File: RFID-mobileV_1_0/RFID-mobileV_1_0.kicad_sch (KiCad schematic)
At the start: 5 parts

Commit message: 增加電池管理IC
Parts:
- removed F?: Fuse, Fuse:Fuse_0805_2012Metric, symbol Device:Fuse
- added U?: (no value), Package_TO_SOT_SMD:TSOT-23-5, symbol Battery_Management:TP4054
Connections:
- net +5V: now also J?.A4 (VBUS), J?.A9 (VBUS), J?.B4 (VBUS), J?.B9 (VBUS)
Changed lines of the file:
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@@
     (stroke (width 0) (type solid) (color 0 0 0 0))
   )
-  (wire (pts (xy 39.37 20.32) (xy 42.291 20.32))
-    (stroke (width 0) (type solid) (color 0 0 0 0))
-  )
-  (wire (pts (xy 49.911 20.32) (xy 52.07 20.32))
+  (wire (pts (xy 39.37 20.32) (xy 52.07 20.32))
     (stroke (width 0) (type solid) (color 0 0 0 0))
   )
@@
     (pin "S1")
   )
-  (symbol (lib_id "Device:Fuse") (at 46.101 20.32 90) (unit 1)
-    (in_bom yes) (on_board yes)
-    (property "Reference" "F?" (id 0) (at 46.101 15.3478 90))
-    (property "Value" "Fuse" (id 1) (at 46.101 17.6465 90))
-    (property "Footprint" "Fuse:Fuse_0805_2012Metric" (id 2) (at 46.101 22.098 90)
-      (effects (font (size 1.27 1.27)) hide)
-    )
-    (property "Datasheet" "~" (id 3) (at 46.101 20.32 0)
-      (effects (font (size 1.27 1.27)) hide)
-    )
-    (property "LCSC" "C135327" (id 4) (at 46.355 22.225 90))
-    (pin "1")
-    (pin "2")
-  )
   (symbol (lib_id "power:PWR_FLAG") (at 59.69 20.32 0) (unit 1)
     (in_bom yes) (on_board yes)
@@
     )
     (pin "1")
+  )
+  (symbol (lib_id "Battery_Management:TP4054") (at 76.2 135.255 0) (unit 1)
+    (in_bom yes) (on_board yes) (fields_autoplaced)
+    (property "Reference" "U?" (id 0) (at 85.725 127 0))
+    (property "Value" "" (id 1) (at 85.725 129.54 0))
+    (property "Footprint" "Package_TO_SOT_SMD:TSOT-23-5" (id 2) (at 87.63 144.145 0)
+      (effects (font (size 1.27 1.27)) hide)
+    )
+    (property "Datasheet" "" (id 3) (at 99.06 149.225 0)
+      (effects (font (size 1.27 1.27)) hide)
+    )
+    (property "LCSC" "C32574" (id 4) (at 96.52 131.445 0)
+      (effects (font (size 1.27 1.27)) (justify right) hide)
+    )
+    (pin "1")
+    (pin "2")
+    (pin "3")
+    (pin "4")
+    (pin "5")
   )
   (sheet_instances
@@
       (reference "BT?") (unit 1) (value "Battery") (footprint "")
     )
-    (path "/a647641f-bf16-4177-91ee-b01f347ff91c"
-      (reference "F?") (unit 1) (value "Fuse") (footprint "Fuse:Fuse_0805_2012Metric")
-    )
     (path "/a49e8613-3cd2-48ed-8977-6bb5023f7722"
       (reference "J?") (unit 1) (value "USB_C_Receptacle_USB2.0") (footprint "Connector_USB:USB_C_Receptacle_HRO_TYPE-C-31-M-12")
@@
       (reference "R?") (unit 1) (value "5K1") (footprint "Resistor_SMD:R_0805_2012Metric")
     )
-  )
+    (path "/cdc7c457-e16e-4018-ab8d-ab6698e85393"
+      (reference "U?") (unit 1) (value "TP4054") (footprint "Package_TO_SOT_SMD:TSOT-23-5")
+    )
+  )

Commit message: update sch
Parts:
- added BZ?: Buzzer, Buzzer_Beeper:Buzzer_Murata_PKLCS1212E, symbol Device:Buzzer
- added Q?: MMBT3904, Package_TO_SOT_SMD:SOT-23, symbol Transistor_BJT:MMBT3904
- added R?: 1k, Resistor_SMD:R_0805_2012Metric, symbol Device:R
- added R?: 22k, Resistor_SMD:R_0805_2012Metric, symbol Device:R
- added U?: (no value), symbol MCU_ST_STM32G0:STM32G030FxP
- added U?: (no value), symbol RF_Module:E220-400TxxS
- added U?: (no value), Package_TO_SOT_SMD:SOT-23-5, symbol Battery_Management:DW02
- BT?: value (none) -> Battery
- U?: value (none) -> TP4054
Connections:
- net +5V: now also BZ?.1 (-), R?.2
- net GND: now also Q?.2 (E)
- new net: BZ?.2 (+), Q?.3 (C), R?.1
- new net: Q?.1 (B), R?.1
- new net buz: R?.2

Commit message: Update RFID-mobileV_1_0.kicad_sch
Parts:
- U?: footprint (none) -> Package_SO:TSSOP-20_4.4x6.5mm_P0.65mm
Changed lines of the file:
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@@
     (property "Reference" "U?" (id 0) (at 142.875 30.48 0))
     (property "Value" "" (id 1) (at 142.875 33.02 0))
-    (property "Footprint" "" (id 2) (at 185.42 86.36 0)
+    (property "Footprint" "Package_SO:TSSOP-20_4.4x6.5mm_P0.65mm" (id 2) (at 185.42 86.36 0)
       (effects (font (size 1.27 1.27)) hide)
     )

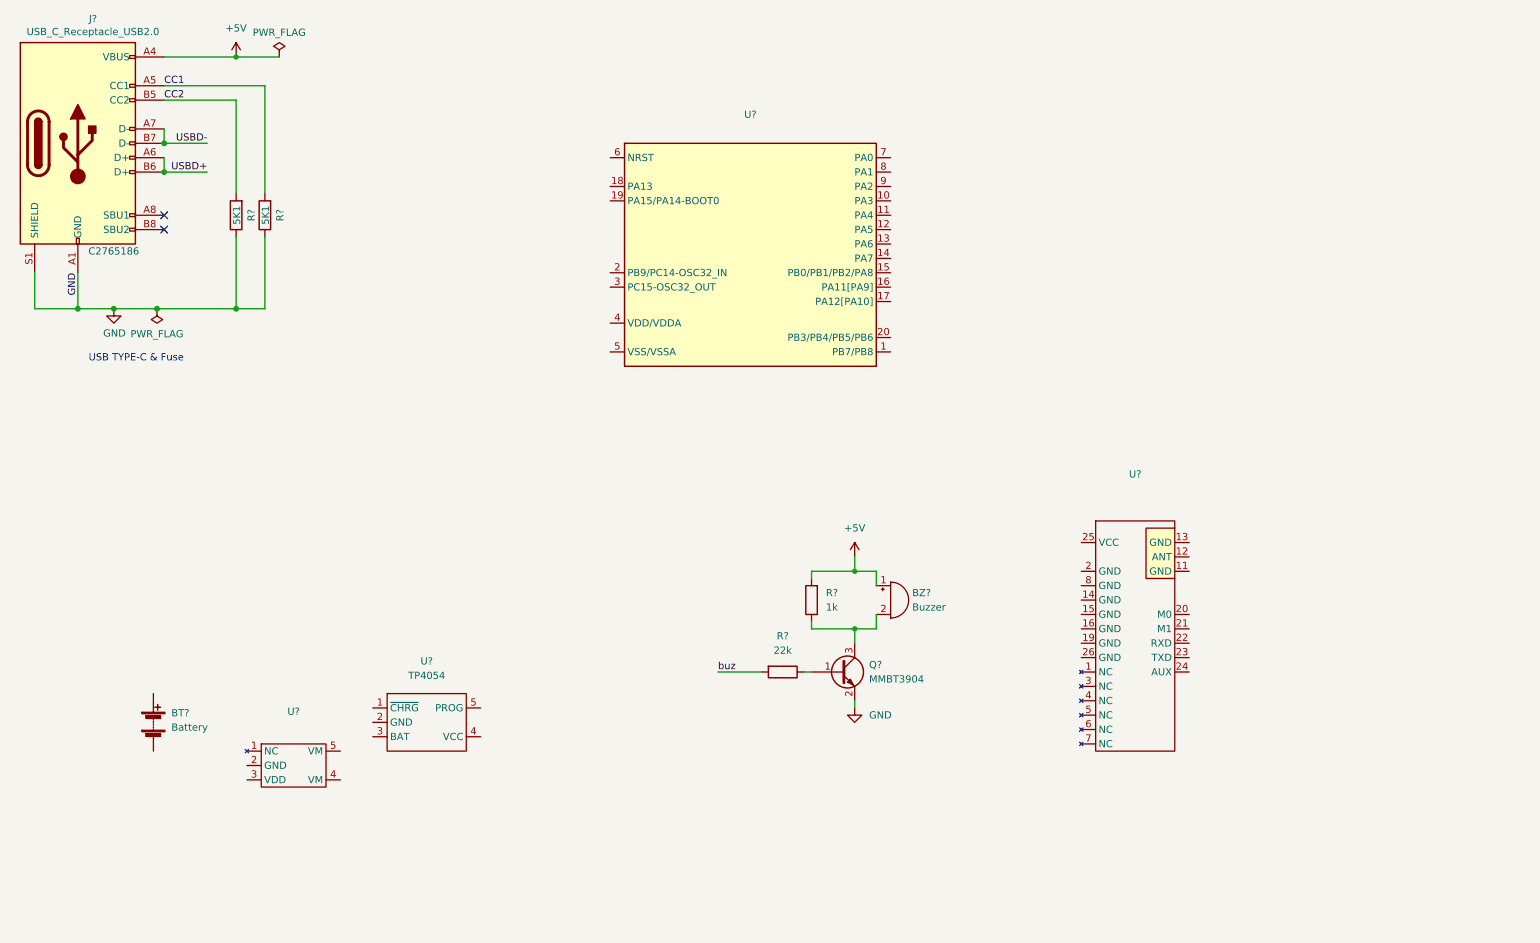
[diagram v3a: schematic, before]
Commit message: add ign update sch
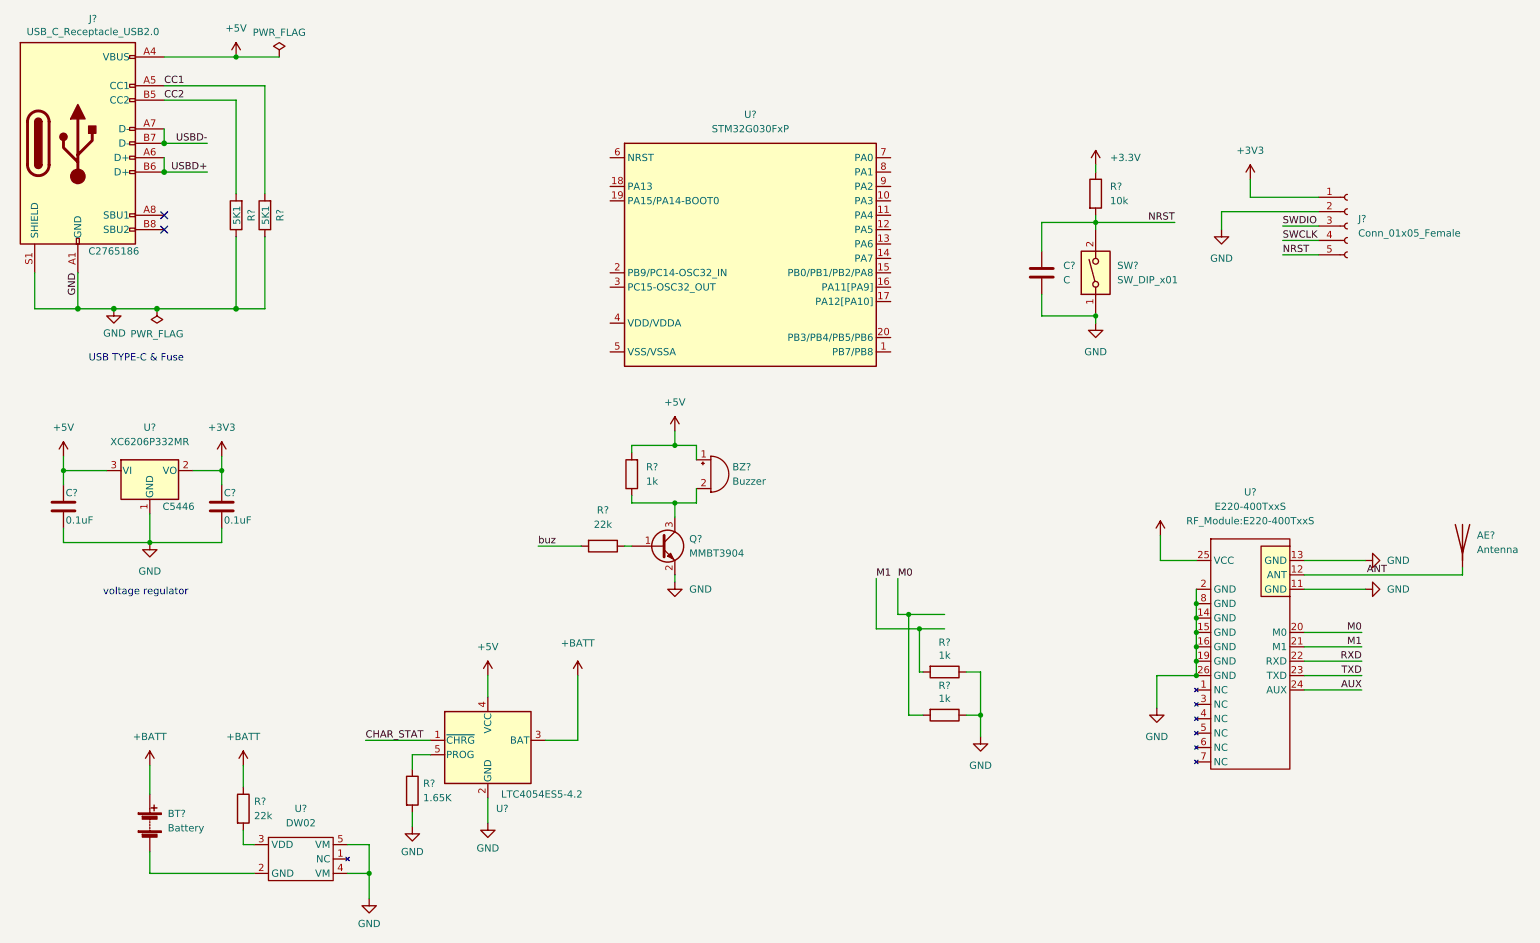
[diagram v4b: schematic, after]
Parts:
- removed U?: (no value), symbol RF_Module:E220-400TxxS
- removed U?: TP4054, Package_TO_SOT_SMD:TSOT-23-5, symbol Battery_Management:TP4054
- removed U?: (no value), Package_TO_SOT_SMD:SOT-23-5, symbol Battery_Management:DW02
- added AE?: Antenna, RF_Antenna:433MHz, symbol Device:Antenna
- added C?: C, symbol Device:C
- added C? (x2): 0.1uF, Capacitor_SMD:C_0805_2012Metric, symbol Device:C
- added J?: Conn_01x05_Female, Connector_Harwin:Harwin_M20-89005xx_1x05_P2.54mm_Horizontal, symbol Connector:Conn_01x05_Female
- added R? (x2): 1k, Resistor_SMD:R_0805_2012Metric, symbol Device:R
- added R?: 1.65K, Resistor_SMD:R_0805_2012Metric, symbol Device:R
- added R?: 22k, Resistor_SMD:R_0805_2012Metric, symbol Device:R
- added R?: 10k, Resistor_SMD:R_0805_2012Metric, symbol Device:R
- added SW?: SW_DIP_x01, Button_Switch_SMD:SW_DIP_SPSTx01_Slide_6.7x4.1mm_W8.61mm_P2.54mm_LowProfile, symbol Switch:SW_DIP_x01
- added U?: LTC4054ES5-4.2, Package_TO_SOT_SMD:TSOT-23-5, symbol Battery_Management:LTC4054ES5-4.2
- added U?: E220-400TxxS, RF_Module:E220-400TxxS, symbol RF_Module:E220-400TxxS
- added U?: XC6206P332MR, Package_TO_SOT_SMD:SOT-23, symbol Regulator_Linear:XC6206PxxxMR
- added U?: DW02, Package_TO_SOT_SMD:SOT-23-5, symbol Battery_Management:DW02
- U?: value (none) -> STM32G030FxP
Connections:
- net +5V: now also C?.1, U?.3 (VI), U?.4 (VCC)
- net GND: now also C?.2, C?.2, C?.2, J?.2 (Pin_2), R?.1, R?.1, R?.2, SW?.1, U?.1 (GND), U?.11 (GND), U?.13 (GND), U?.14 (GND), U?.15 (GND), U?.16 (GND), U?.19 (GND), U?.2 (GND), U?.2 (GND), U?.26 (GND), U?.4 (VM), U?.5 (VM), U?.8 (GND)
- net +BATT: now reaches BT?.1 (+)
- net +BATT: now also R?.1, U?.25 (VCC), U?.3 (BAT)
- net at BT?.2 (-): now also U?.2 (GND)
- new net: R?.1, U?.5 (PROG)
- new net: R?.2, U?.3 (VDD)
- new net +3V3: C?.1, J?.1 (Pin_1), R?.1, U?.2 (VO)
- new net ANT: AE?.1 (A), U?.12 (ANT)
- new net AUX: U?.24 (AUX)
- new net CHAR_STAT: U?.1 (~{CHRG})
- new net M0: R?.2, U?.20 (M0)
- new net M1: R?.2, U?.21 (M1)
- new net NRST: C?.1, J?.5 (Pin_5), R?.2, SW?.2
- new net RXD: U?.22 (RXD)
- new net SWCLK: J?.4 (Pin_4)
- new net SWDIO: J?.3 (Pin_3)
- new net TXD: U?.23 (TXD)
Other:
- note added: "voltage regulator"
- moved on the sheet: BT?, BZ?, Q?, R?

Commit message: Update RFID-mobileV_1_0.kicad_sch
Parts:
- added C? (x2): 0.1uF, Capacitor_SMD:C_0805_2012Metric, symbol Device:C
- added J?: (no value), symbol Connector:Conn_01x05_Male
- added J?: Conn_01x05_Male, Connector_PinHeader_2.54mm:PinHeader_1x05_P2.54mm_Vertical, symbol Connector:Conn_01x05_Male
- added JP? (x2): (no value), symbol Jumper:SolderJumper_2_Open
- added JP? (x2): SolderJumper_2_Open, symbol Jumper:SolderJumper_2_Open
- added R? (x2): 22k, Resistor_SMD:R_0805_2012Metric, symbol Device:R
- added R?: (no value), symbol Device:R
- added U?: (no value), symbol Amplifier_Operational:LM321
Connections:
- net +3V3: now also BZ?.1 (-), R?.2, U?.4 (VDD/VDDA), C?.1, J?.1 (Pin_1), J?.1 (Pin_1), JP?.2 (B), JP?.2 (B), R?.1
- net +5V: now also C?.1; no longer BZ?.1 (-), R?.2
- net +BATT: now also R?.1, U?.5 (V+)
- net CHAR_STAT: now also U?.8 (PA1), R?.2
- net GND: now also U?.5 (VSS/VSSA), C?.2, C?.2, J?.5 (Pin_5), J?.5 (Pin_5), R?.2, U?.2 (V-)
- net M0: now also R?.2, JP?.1 (A); no longer R?.2
- net M1: now also R?.2, JP?.1 (A); no longer R?.2
- net NRST: now also U?.6 (NRST)
- net SWCLK: now also U?.19 (PA15/PA14-BOOT0)
- net SWDIO: now also U?.18 (PA13)
- net RFID_TXD_: now reaches U?.1 (PB7/PB8)
- net RFID_TXD_: now also J?.2 (Pin_2)
- net LoRa_TXD: now reaches U?.10 (PA3)
- net LoRa_TXD: now also JP?.2 (B)
- net RFID_RXD_: now reaches U?.20 (PB3/PB4/PB5/PB6)
- net RFID_RXD_: now also J?.3 (Pin_3)
- net BATT_moint: now reaches U?.7 (PA0)
- net BATT_moint: now also U?.3 (-), U?.4
- net LoRa_RXD: now reaches U?.9 (PA2)
- net LoRa_RXD: now also JP?.2 (B)
- net RXD renamed LoRa_RXD_
- net LoRa_RXD_: now also J?.3 (Pin_3), JP?.1 (A)
- net TXD renamed LoRa_TXD_
- net LoRa_TXD_: now also J?.2 (Pin_2), JP?.1 (A)
- new net: R?.1, R?.2, U?.1 (+)
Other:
- moved on the sheet: AE?, BT?, BZ?, C?, J?, Q?, R?, SW?, U?

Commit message: Update RFID-mobileV_1_0.kicad_sch
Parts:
- U?: LCSC (none) -> C7972
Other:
- moved on the sheet: BT?, BZ?, C?, Q?, R?, U?

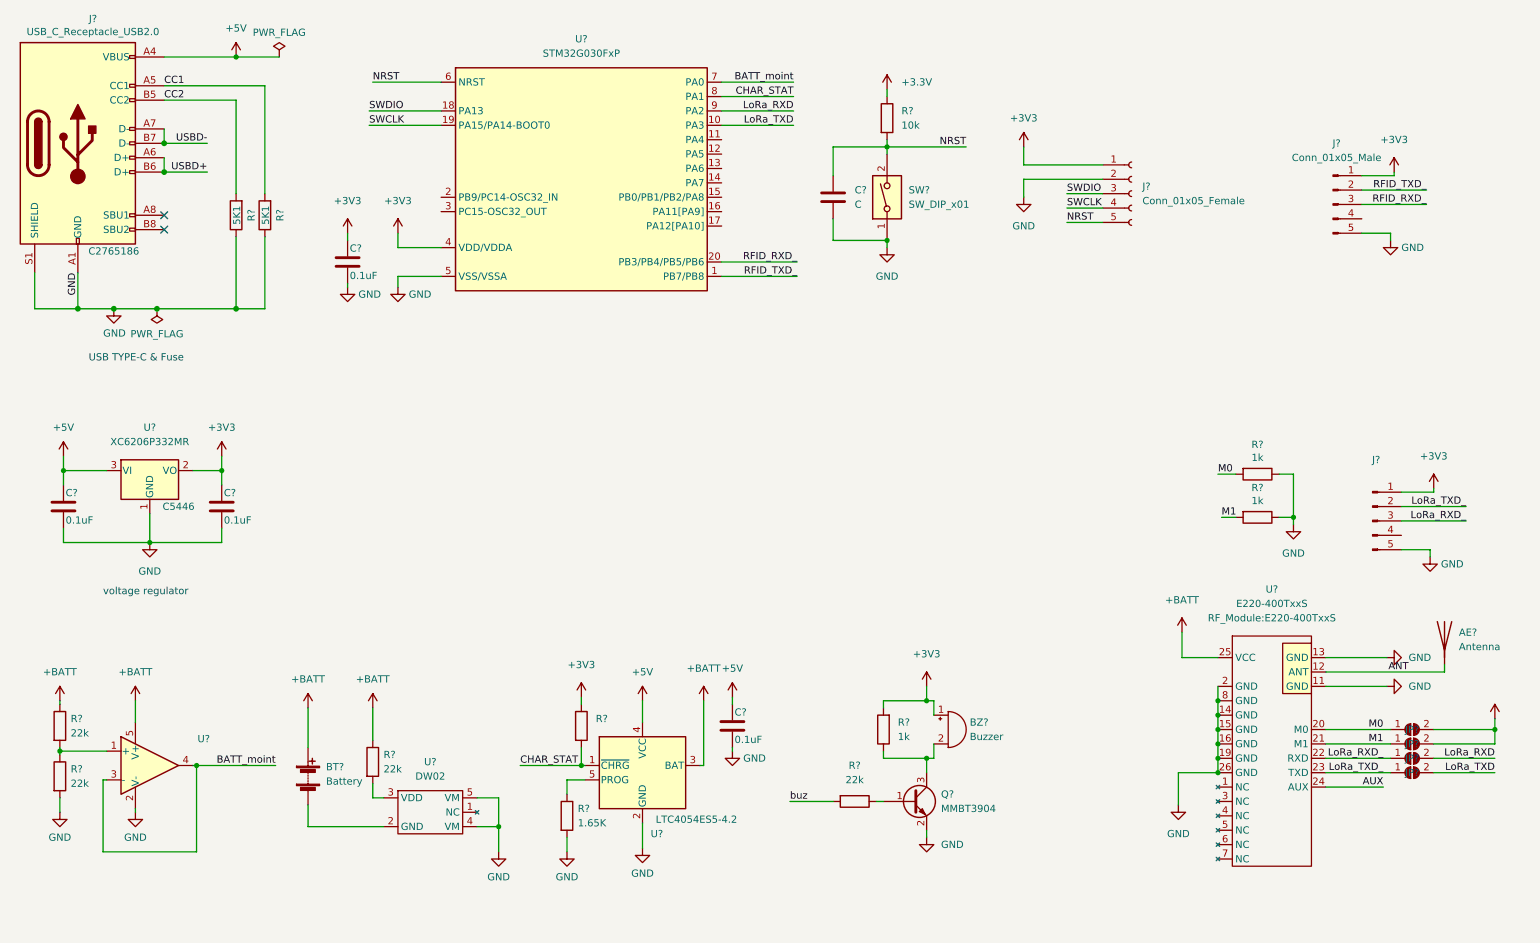
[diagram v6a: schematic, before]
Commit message: Update RFID-mobileV_1_0.kicad_sch
AUX pin
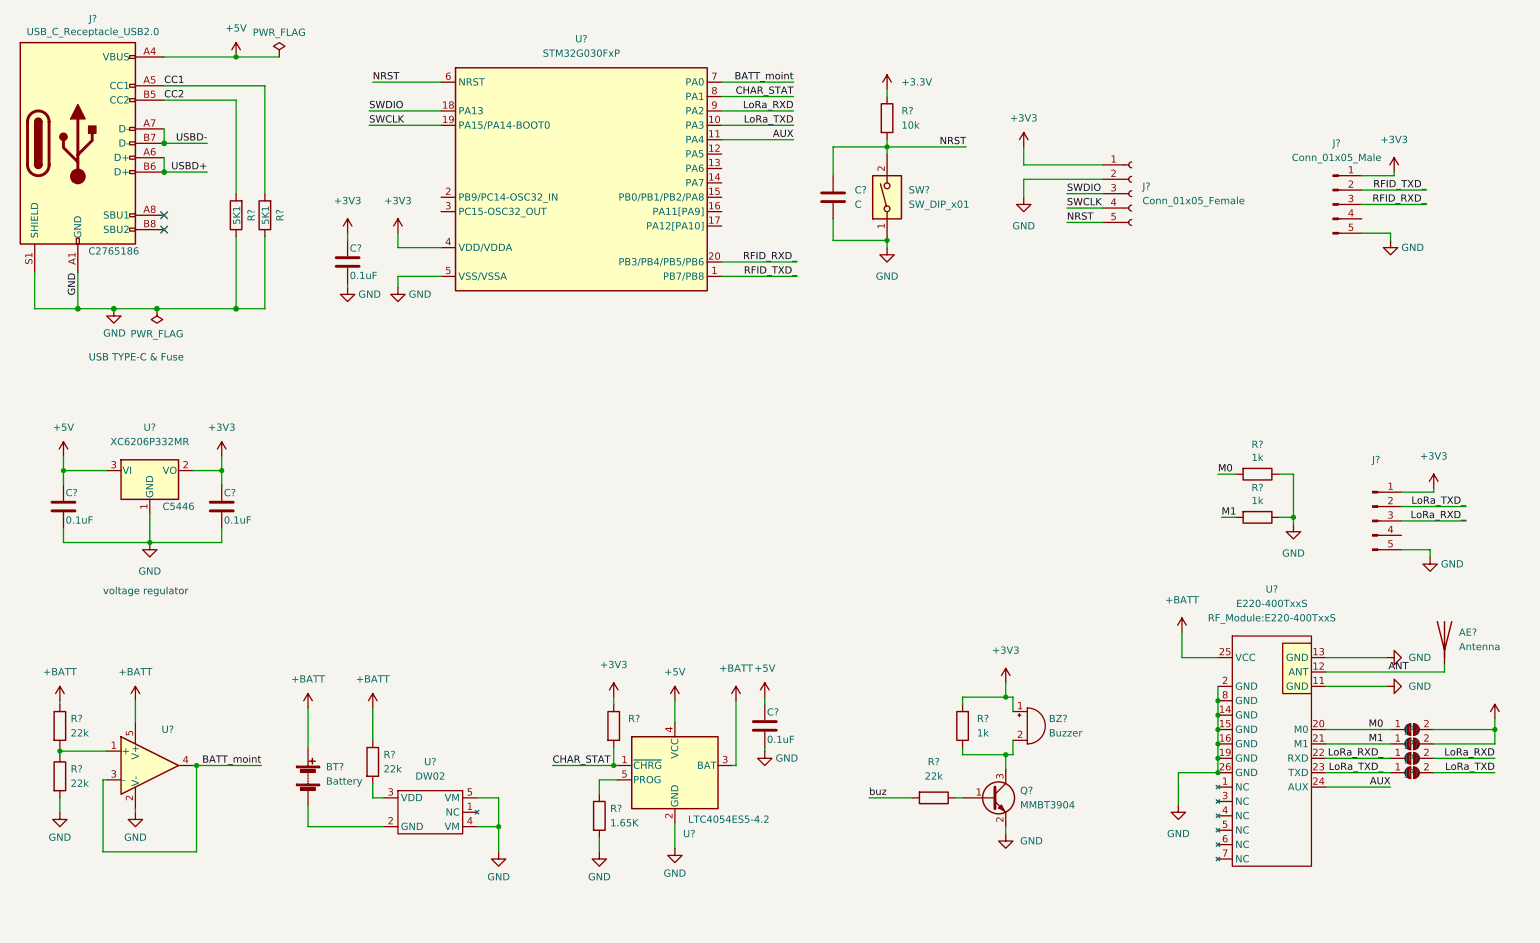
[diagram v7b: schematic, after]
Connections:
- net AUX: now also U?.11 (PA4)
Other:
- moved on the sheet: BZ?, C?, Q?, R?, U?

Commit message: Update RFID-mobileV_1_0.kicad_sch
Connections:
- net AUX renamed LoRa_AUX
- no-connect marks 2 -> 5
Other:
- moved on the sheet: BZ?, J?, Q?, R?
